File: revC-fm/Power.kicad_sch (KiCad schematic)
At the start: 55 parts, among them Q15 MMDT5551-7-F, Q16 MMDT5551-7-F, Q18 IRF7404TRPBF, Q32 MMBT4403WT1G, SW3 USB Charge Inhibit, SW4 High Inhibit, SW5 High USB Inhibit, SW6 Low Inhibit, U18 TPS54226PWPRPWP14_2P31X2P46-L, U19 ADM1176-1ARMZ-R7, U20 ADM1176-1ARMZ-R7, U21 BQ25883RGER

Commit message: working revC
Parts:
- removed MES1: U70, symbol Device:Ammeter_DC
- removed MES2: U68, symbol Device:Ammeter_DC
- removed R136: CUBESAT LOAD, symbol Device:R_US
- removed SW3: USB Charge Inhibit, symbol Switch:SW_SPST
- removed SW4: High Inhibit, symbol Switch:SW_SPST
- removed SW5: High USB Inhibit, symbol Switch:SW_SPST
- removed SW6: Low Inhibit, symbol Switch:SW_SPST
- added C10, C8, C9: 3.3nF, Capacitor_SMD:C_0603_1608Metric, symbol Device:C
- added R10, R12, R9: 1k, Resistor_SMD:R_0603_1608Metric, symbol Device:R_US
- added R11, R7, R8: 47mR, mainboard-SLI:KRL3216, symbol Device:R_US
- added R27, R6: 150k, Resistor_SMD:R_0603_1608Metric, symbol Device:R_US
- added U5, U8, U9: ADM1176-1ARMZ-R7, mainboard:ADM1176-1ARMZ-R7, symbol mainboard:ADM1176-1ARMZ-R7
- R137, R138: value 0.1 -> 47mR; footprint Resistor_SMD:R_2512_6332Metric -> mainboard-SLI:KRL3216
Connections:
- net 3.3V: now also R10.1, R7.1, U5.2 (SENSE); no longer C61.2, C62.2, L3.2
- net GND: now also C10.1, C8.1, C9.1, R27.1, R6.1, U5.4 (GND), U5.8 (A0), U8.4 (GND), U8.9 (A1), U9.4 (GND)
- net SCL_PWR: now also U5.6 (SCL), U8.6 (SCL), U9.6 (SCL)
- net SDA_PWR: now also U5.7 (SDA), U8.7 (SDA), U9.7 (SDA)
- net VCC_PAYLOAD: now also R8.1, R9.1, U8.2 (SENSE)
- net at U20.8 (A0): now also R27.2
- new net: R9.2, U8.3 (ON)
- new net: C9.2, U8.5 (TIMER)
- new net: R12.2, U9.3 (ON)
- new net: C10.2, U9.5 (TIMER)
- new net: R10.2, U5.3 (ON)
- new net: R6.2, U5.9 (A1)
- new net: C8.2, U5.5 (TIMER)
- new net 3.3Vout: C61.2, C62.2, L3.2, R7.2, U5.1 (VCC)
- new net 5V Payload Regulator/Vout: R8.2, U8.1 (VCC)
- new net 5V RF Regulator/Vout: R11.2, U9.1 (VCC)
- new net 5V_RF: R11.1, R12.1, U9.2 (SENSE), U9.8 (A0), U9.9 (A1)
- no-connect marks 8 -> 11
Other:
- note added: "Addr: 0x41"
- note added: "Addr: 0x42"
- note added: "Addr: 0x43"
- note added: "Addr: 0x44"
- note added: "Addr: 0x48"
- note added: "power to battery node from solar charger"
- note removed: "5V_USB"
- note removed: "Addr: 0x90"
- note removed: "Addr: 0x94"
- note removed: "Current Sense Resistor: 1.0 Ohm is about 0.3mW power lost as heat"
- note removed: "GND"
- note removed: "GNDREF"
- note removed: "SYMBOLIC POWER DIAGRAM"
- note removed: "Solar Reg"
- note removed: "USB Bus Reg"
- note removed: "USB Charge Reg"
- note removed: "USB_RET"
- note removed: "VBATT"
- note removed: "VBUS"
- note removed: "VBUS_INHIBIT"
- note removed: "VBUS_USB"
- note removed: "VCHRG"
- note removed: "VCHRG_USB"
- note removed: "VSOLAR"
- note removed: "VSOLAR_RET"
- note removed: "power TO battery node"
- note removed: "to get battery charging current, subtract u68 current from u68 current"
- moved on the sheet: C61, C62, C63, C64, C65, C66, C67, C68, C69, C70, C71, C72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

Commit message: working revC
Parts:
- added C69, C70: 47uF, Capacitor_SMD:C_1206_3216Metric, symbol Device:C
- C67: renamed from C63; value 100uF -> 47uF; footprint Capacitor_SMD:C_1210_3225Metric -> Capacitor_SMD:C_1206_3216Metric
- C68: renamed from C64; value 100uF -> 47uF; footprint Capacitor_SMD:C_1210_3225Metric -> Capacitor_SMD:C_1206_3216Metric
- Q19: renamed from Q18; value IRF7404TRPBF -> BSZ180P03NS3GATMA1; footprint Package_SO:SOIC-8_3.9x4.9mm_P1.27mm -> mainboard-SLI:PG-TSDSON-8_3.3x3.3mm; symbol mainboard_SLI:IRF7404TRPBF -> mainboard_SLI:BSZ180; Flight IRF7404TRPBF -> (none)
- R23: value 100 -> 1k
- renumbered C69 to C51, C9 to C52, C10 to C53, C70 to C54, C71 to C55, C73 to C56, C68 to C57, C75 to C58, C77 to C59, C76 to C60, C74 to C63, C72 to C64, C67 to C71, C8 to C72, L4 to L3, L3 to L4, Q15 to Q16, Q16 to Q18, R137 to R108, R141 to R109, R8 to R110, R9 to R111, R11 to R112, R12 to R113, R138 to R114, R142 to R115, R27 to R116, R140 to R117, R144 to R118, R147 to R119, R148 to R120, R155 to R121, R149 to R123, R146 to R125, R150 to R126, R151 to R127, R152 to R128, R154 to R129, R145 to R130, R156 to R131, R139 to R132, R143 to R133, R7 to R134, R10 to R135, R6 to R136, U19 to U12, U8 to U13, U9 to U14, U20 to U15, U21 to U16, U18 to U17, U5 to U18
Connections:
- net 3.3V: no longer Q19.2 (S), Q19.3 (S)
- net GND: now also C69.2, C70.2
- net GPS_PWR_IN: no longer Q19.6 (D), Q19.7 (D), Q19.8 (D)
- net VBUS: now also C69.1, C70.1
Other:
- note removed: "16V ceramic 1210 caps"
- moved on the sheet: C61, C62, C67, C68, Q32, R121, R195, R23

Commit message: working revC
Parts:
- removed Q19: BSZ180P03NS3GATMA1, mainboard-SLI:PG-TSDSON-8_3.3x3.3mm, symbol mainboard_SLI:BSZ180
- removed Q32: MMBT4403WT1G, Package_TO_SOT_SMD:SOT-323_SC-70, symbol mainboard-rescue:Q_PNP_BEC-Device-mainboard-rescue
- removed R121: 1Meg, Resistor_SMD:R_0603_1608Metric, symbol Device:R_US
- removed R195: 10Meg, Resistor_SMD:R_0603_1608Metric, symbol Device:R_US
- removed R23: 1k, Resistor_SMD:R_0603_1608Metric, symbol Device:R_US
- L2: renamed from L3; footprint mainboard-SLI:74404032010 -> SierraLobo:74404032010; Flight 74404032010 -> (none); Manufacturer_Part_Number 744316100 -> (none); Proto 744316100 -> (none)
- L3: renamed from L4; footprint mainboard:L_2141 -> SierraLobo:L_2141; Flight SPM5030T-3R3M-HZ -> (none); Manufacturer_Name TAI-TECH -> (none); Manufacturer_Part_Number HPC5040NF-3R3MTH -> (none); Proto HPC5040NF-3R3MTH -> (none)
- Q1: renamed from Q16; symbol mainboard-rescue:MBT2222ADW1T1-Transistor_BJT-mainboard-rescue -> Transistor_BJT:MMDT5551; Flight MMDT5551-7-F -> (none); Manufacturer_Name ON Semiconductor -> (none); Manufacturer_Part_Number MBT2222ADW1T1G -> (none); Proto MBT2222ADW1T1G -> (none)
- Q2: renamed from Q18; symbol mainboard-rescue:MBT2222ADW1T1-Transistor_BJT-mainboard-rescue -> Transistor_BJT:MMDT5551; Flight MMDT5551-7-F -> (none)
- Q2: renamed from Q18; symbol mainboard-rescue:MBT2222ADW1T1-Transistor_BJT-mainboard-rescue -> Transistor_BJT:MMDT5551; Flight MBT2222ADW1T1G -> (none); Manufacturer_Name ON Semiconductor -> (none); Manufacturer_Part_Number MBT2222ADW1T1G -> (none); Proto MBT2222ADW1T1G -> (none)
- R54: renamed from R108; footprint mainboard-SLI:KRL3216 -> SierraLobo:KRL3216
- R56: renamed from R110; footprint mainboard-SLI:KRL3216 -> SierraLobo:KRL3216
- R58: renamed from R112; footprint mainboard-SLI:KRL3216 -> SierraLobo:KRL3216
- R60: renamed from R114; footprint mainboard-SLI:KRL3216 -> SierraLobo:KRL3216
- R77: renamed from R134; footprint mainboard-SLI:KRL3216 -> SierraLobo:KRL3216
- U10: renamed from U12; footprint mainboard:ADM1176-1ARMZ-R7 -> SierraLobo:ADM1176-1ARMZ-R7; symbol mainboard:ADM1176-1ARMZ-R7 -> SierraLobo:ADM1176-1ARMZ-R7; Flight ADM1176-1ARMZ-R7 -> (none); Manufacturer_Name Analog Devices Inc. -> (none); Manufacturer_Part_Number ADM1176-1ARMZ-R7 -> (none); Proto ADM1176-1ARMZ-R7 -> (none)
- U11: renamed from U13; footprint mainboard:ADM1176-1ARMZ-R7 -> SierraLobo:ADM1176-1ARMZ-R7; symbol mainboard:ADM1176-1ARMZ-R7 -> SierraLobo:ADM1176-1ARMZ-R7; Flight ADM1176-1ARMZ-R7 -> (none); Manufacturer_Name Analog Devices Inc. -> (none); Manufacturer_Part_Number ADM1176-1ARMZ-R7 -> (none); Proto ADM1176-1ARMZ-R7 -> (none)
- U12: renamed from U14; footprint mainboard:ADM1176-1ARMZ-R7 -> SierraLobo:ADM1176-1ARMZ-R7; symbol mainboard:ADM1176-1ARMZ-R7 -> SierraLobo:ADM1176-1ARMZ-R7; Flight ADM1176-1ARMZ-R7 -> (none); Manufacturer_Name Analog Devices Inc. -> (none); Manufacturer_Part_Number ADM1176-1ARMZ-R7 -> (none); Proto ADM1176-1ARMZ-R7 -> (none)
- U13: renamed from U15; footprint mainboard:ADM1176-1ARMZ-R7 -> SierraLobo:ADM1176-1ARMZ-R7; symbol mainboard:ADM1176-1ARMZ-R7 -> SierraLobo:ADM1176-1ARMZ-R7; Flight ADM1176-1ARMZ-R7 -> (none); Manufacturer_Name Analog Devices Inc. -> (none); Manufacturer_Part_Number ADM1176-1ARMZ-R7 -> (none); Proto ADM1176-1ARMZ-R7 -> (none)
- U14: renamed from U16; footprint mainboard:QFN50P400X400X100-25N-D -> SierraLobo:QFN50P400X400X100-25N-D; symbol mainboard:BQ25883RGER -> SierraLobo:BQ25883RGER; Flight BQ25883RGER -> (none); Manufacturer_Name Texas Instruments -> (none); Manufacturer_Part_Number BQ25883RGER -> (none); Proto BQ25883RGER -> (none)
- U15: renamed from U17; value TPS54226PWPRPWP14_2P31X2P46-L -> TPS54226PWPR; footprint mainboard:PWP14_2P31X2P46-L -> SierraLobo:PWP14_2P31X2P46-L; symbol mainboard:TPS54226PWPRPWP14_2P31X2P46-L -> SierraLobo:TPS54226PWPR; Flight TPS54226PWPR -> (none); Manufacturer_Name Texas Instruments -> (none); Manufacturer_Part_Number TPS54226PWPR -> (none); Proto TPS54226PWPR -> (none)
- U16: renamed from U18; footprint mainboard:ADM1176-1ARMZ-R7 -> SierraLobo:ADM1176-1ARMZ-R7; symbol mainboard:ADM1176-1ARMZ-R7 -> SierraLobo:ADM1176-1ARMZ-R7; Flight ADM1176-1ARMZ-R7 -> (none); Manufacturer_Name Analog Devices Inc. -> (none); Manufacturer_Part_Number ADM1176-1ARMZ-R7 -> (none); Proto ADM1176-1ARMZ-R7 -> (none)
- renumbered C51 to C29, C52 to C30, C53 to C31, C54 to C32, C55 to C33, C56 to C34, C57 to C35, C58 to C36, C59 to C37, C60 to C38, C61 to C39, C62 to C40, C63 to C41, C64 to C42, C65 to C43, C66 to C44, C67 to C45, C68 to C46, C69 to C47, C70 to C48, C71 to C49, C72 to C50, R109 to R55, R111 to R57, R113 to R59, R115 to R61, R116 to R62, R117 to R63, R118 to R64, R119 to R65, R120 to R66, R123 to R67, R125 to R68, R126 to R69, R127 to R70, R128 to R71, R129 to R72, R130 to R73, R131 to R74, R132 to R75, R133 to R76, R135 to R78, R136 to R79
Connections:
- net 3.3V: now also R77.2; no longer R75.2, R77.1, U15.1 (VO)
- net 3.3Vout: now also R75.2, R77.1, U15.1 (VO); no longer R77.2
- net 5V Payload Regulator/Vout: now also R56.1; no longer R56.2
- net 5V RF Regulator/Vout: now also R58.1; no longer R58.2
- net 5V_RF: now also R58.2; no longer R58.1
- net GND: no longer U11.4 (GND)
- net VCC_PAYLOAD renamed 5V_PYLD
- net 5V_PYLD: now also R56.2; no longer R56.1
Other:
- sheet 5V Payload Regulator ports: added EN, PG, SEN; removed ~{EN}
- sheet 5V RF Regulator ports: added EN, PG, SEN; removed ~{EN}
- note added: "5V Power Monitors"
- note added: "power to VBATT from VCHRG"
- note added: "power to VBUS"
- note removed: "GPS Power Switch"
- note removed: "NOTE: Components labeled "do not install" (DNI) are not populated by default"
- note removed: "power TO bus"
- note removed: "power to battery node from solar charger"
- moved on the sheet: C29, C32, C35, Q1A, Q1B, Q2A, Q2B, R54, R55, R56, R58, R60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

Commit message: routing fm
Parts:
- added D6 (x2): SBRT5A50SA-13, Diode_SMD:D_SMA, symbol mainboard-rescue:D_Schottky-Device-mainboard-rescue
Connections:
- net GND: now also D6.2 (A), D6.2 (A)
- net VBATT: now also D6.1 (K)
- net VBUS_INHIBIT: now also D6.1 (K)
- net 5V Payload Regulator/Vout renamed 5V Payload Regulator/VOUT
- net 5V RF Regulator/Vout renamed 5V RF Regulator/VOUT
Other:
- added sheet Temp Sensor 3 (temp_senkicad_sch.kicad_sch)
- sheet 5V Payload Regulator ports: added TEMP, VIN, VIO, VOUT; removed NTC, SEN, Vout
- sheet 5V RF Regulator ports: added TEMP, VIN, VIO, VOUT; removed NTC, SEN, Vout
- sheet Solar Charge Regulator ports: added BATT_NTC, CHRG, SHDN, TEMP, VCHRG, VIN, VIO; removed none
- moved on the sheet: C29, C32, R54, R55, R60, R61, R62, U10, U13

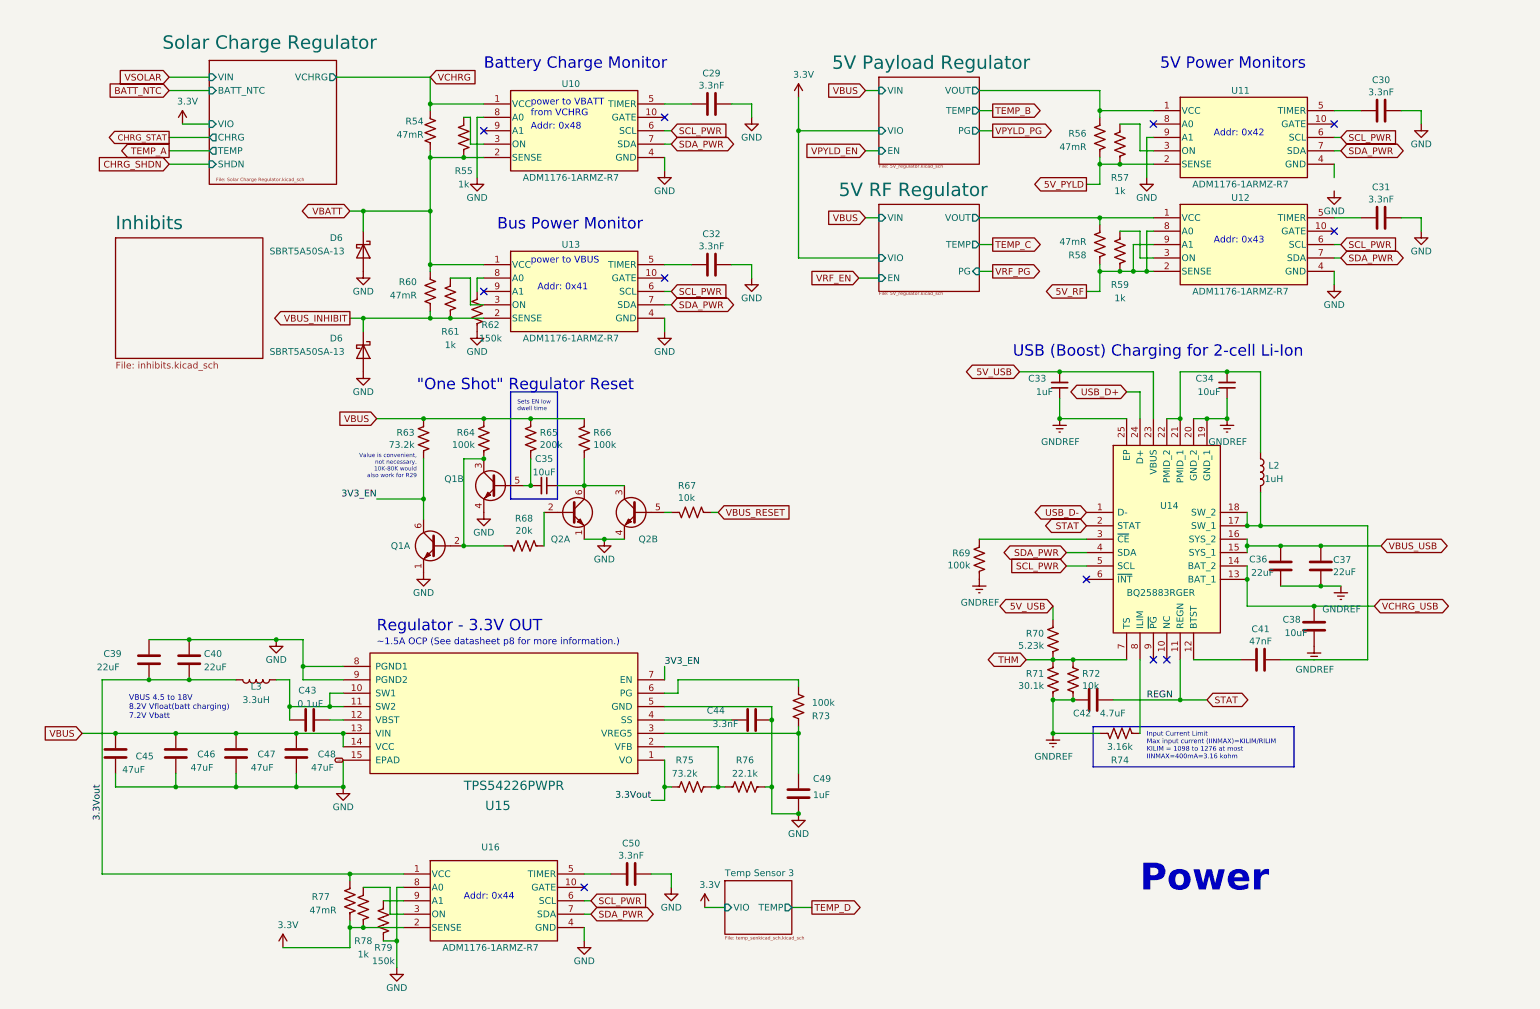
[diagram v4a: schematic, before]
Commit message: updated analog , solar comp, layout
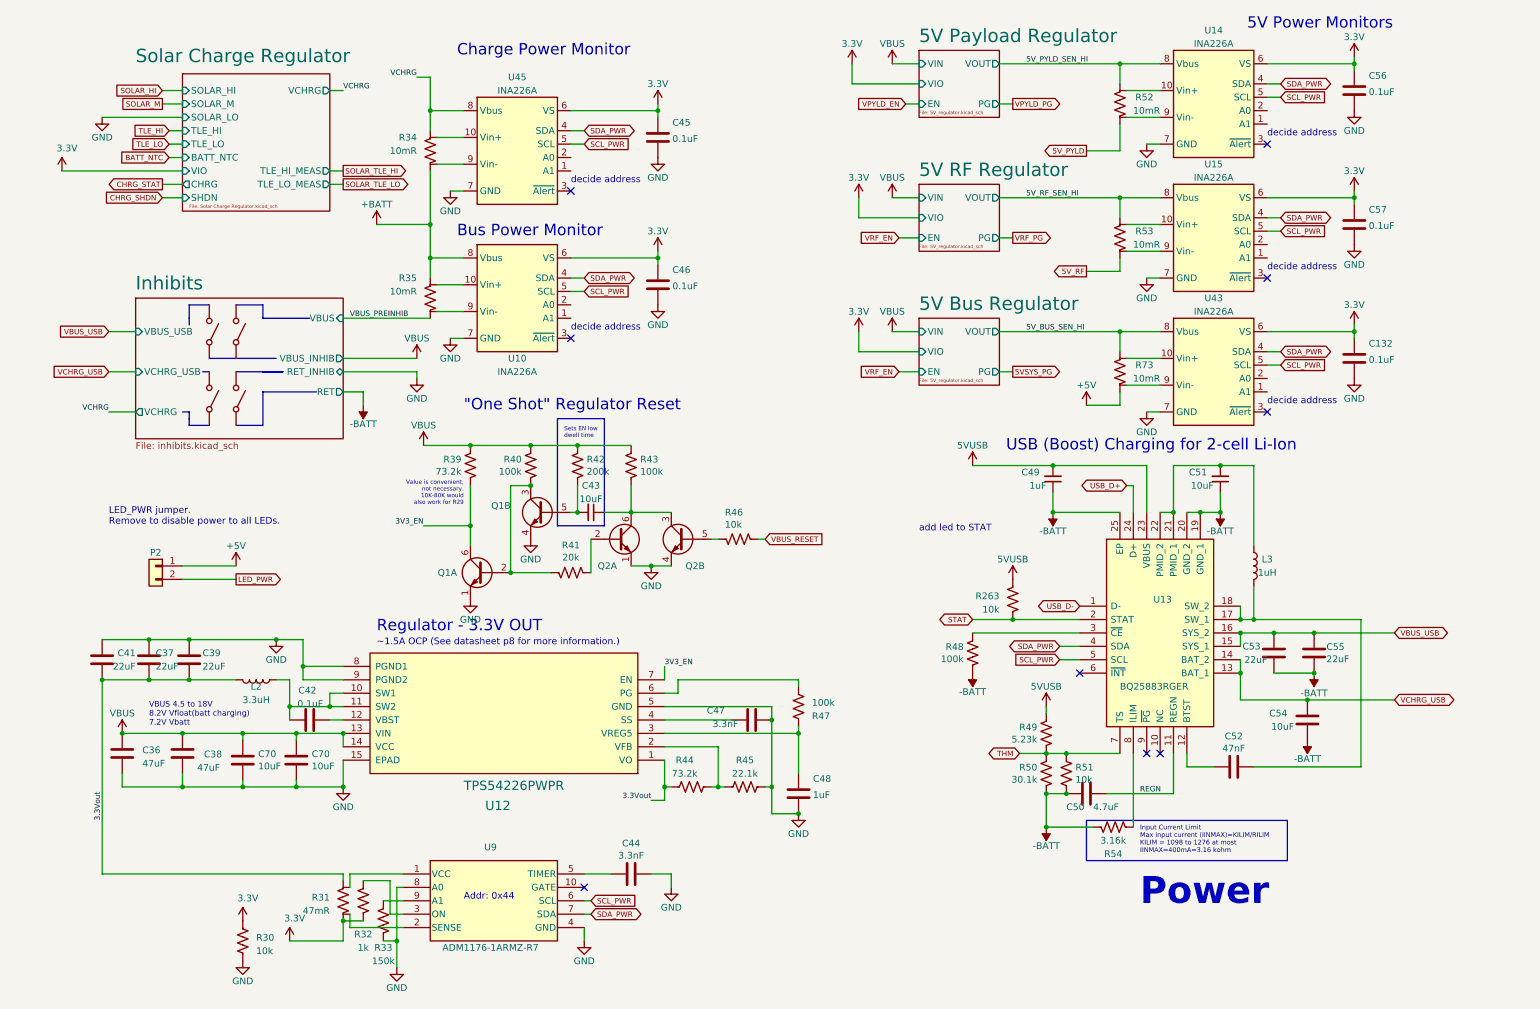
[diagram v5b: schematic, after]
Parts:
- removed C29, C30, C31, C32: 3.3nF, Capacitor_SMD:C_0603_1608Metric, symbol Device:C
- removed C47, C48: 47uF, Capacitor_SMD:C_1206_3216Metric, symbol Device:C
- removed D6 (x2): SBRT5A50SA-13, Diode_SMD:D_SMA, symbol mainboard-rescue:D_Schottky-Device-mainboard-rescue
- removed R55, R57, R59, R61: 1k, Resistor_SMD:R_0603_1608Metric, symbol Device:R_US
- removed R62: 150k, Resistor_SMD:R_0603_1608Metric, symbol Device:R_US
- removed U10, U11, U12, U13: ADM1176-1ARMZ-R7, SierraLobo:ADM1176-1ARMZ-R7, symbol SierraLobo:ADM1176-1ARMZ-R7
- added C132, C45, C46, C56, C57: 0.1uF, Capacitor_SMD:C_0402_1005Metric, symbol Device:C
- added C41: 22uF, Capacitor_SMD:C_0805_2012Metric, symbol Device:C
- added C70 (x2): 10uF, Capacitor_SMD:C_0805_2012Metric, symbol Device:C
- added P2: TSM-102-01-L-SV-P-TR, Connector_PinHeader_2.54mm:PinHeader_1x02_P2.54mm_Vertical_SMD_Pin1Right, symbol Connector_Generic:Conn_01x02
- added R263, R30: 10k, Resistor_SMD:R_0603_1608Metric, symbol Device:R_US
- added R73: 10mR, SierraLobo:KRL3216, symbol SierraLobo:R_US_SENSE
- added SW3, SW4, SW5, SW6: SW_SPST, symbol Switch:SW_SPST
- added U10, U14, U15, U43, U45: INA226A, Package_SO:VSSOP-10_3x3mm_P0.5mm, symbol SierraLobo:INA226A
- C42: renamed from C43; footprint Capacitor_SMD:C_0603_1608Metric -> Capacitor_SMD:C_0402_1005Metric
- C44: renamed from C50; footprint Capacitor_SMD:C_0603_1608Metric -> Capacitor_SMD:C_0402_1005Metric
- C47: renamed from C44; footprint Capacitor_SMD:C_0603_1608Metric -> Capacitor_SMD:C_0402_1005Metric
- C52: renamed from C41; footprint Capacitor_SMD:C_0603_1608Metric -> Capacitor_SMD:C_0402_1005Metric
- L2: renamed from L3; footprint SierraLobo:L_2141 -> Inductor_SMD:L_Wuerth_HCI-5040
- R31: renamed from R77; symbol Device:R_US -> SierraLobo:R_US_SENSE
- R34: renamed from R54; value 47mR -> 10mR; symbol Device:R_US -> SierraLobo:R_US_SENSE
- R35: renamed from R60; value 47mR -> 10mR; symbol Device:R_US -> SierraLobo:R_US_SENSE
- R52: renamed from R56; value 47mR -> 10mR; symbol Device:R_US -> SierraLobo:R_US_SENSE
- R53: renamed from R58; value 47mR -> 10mR; symbol Device:R_US -> SierraLobo:R_US_SENSE
- renumbered C45 to C36, C39 to C37, C46 to C38, C40 to C39, C35 to C43, C49 to C48, C33 to C49, C42 to C50, C34 to C51, C36 to C53, C38 to C54, C37 to C55, L2 to L3, R78 to R32, R79 to R33, R63 to R39, R64 to R40, R68 to R41, R65 to R42, R66 to R43, R75 to R44, R76 to R45, R67 to R46, R73 to R47, R69 to R48, R70 to R49, R71 to R50, R72 to R51, R74 to R54, U15 to U12, U14 to U13, U16 to U9
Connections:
- net 5V Payload Regulator/VOUT is gone; now on net 5V_PYLD: R52.1
- net 5V RF Regulator/VOUT is gone; now on net 5V_RF: R53.1
- net 3.3V: now also R31.1, C132.1, C45.1, C46.1, C56.1, C57.1, R30.1, U10.6 (VS), U14.6 (VS), U15.6 (VS), U43.6 (VS), U45.6 (VS); no longer R31.2, U9.2 (SENSE)
- net 3.3Vout: now also R31.2, C41.2; no longer R31.1, U9.1 (VCC)
- net 5V_PYLD: no longer R52.2
- net 5V_RF: no longer R53.2
- net GND: now also C132.2, C41.1, C45.2, C46.2, C56.2, C57.2, C70.2, C70.2, R30.2, U10.7 (GND), U14.7 (GND), U15.7 (GND), U43.7 (GND), U45.7 (GND)
- net SCL_PWR: now also U10.5 (SCL), U14.5 (SCL), U15.5 (SCL), U43.5 (SCL), U45.5 (SCL)
- net SDA_PWR: now also U10.4 (SDA), U14.4 (SDA), U15.4 (SDA), U43.4 (SDA), U45.4 (SDA)
- net STAT: now also R263.1; no longer C50.1, U13.11 (REGN)
- net VBUS: now also C70.1, C70.1
- net VCHRG: now also U45.8 (Vbus)
- net 5V_USB renamed +5V
- net +5V: now also P2.1 (Pin_1), R263.2, R73.1
- net GNDREF renamed -BATT
- net VBATT renamed +BATT
- net +BATT: now also U10.8 (Vbus)
- net VBUS_INHIBIT renamed VBUS_PREINHIB
- new net: R35.3, U10.9 (Vin-)
- new net: R35.4, U10.10 (Vin+)
- new net: R34.3, U45.9 (Vin-)
- new net: R34.4, U45.10 (Vin+)
- new net: R52.4, U14.10 (Vin+)
- new net: R52.3, U14.9 (Vin-)
- new net: R73.3, U43.9 (Vin-)
- new net: R73.4, U43.10 (Vin+)
- new net: R53.4, U15.10 (Vin+)
- new net: R53.3, U15.9 (Vin-)
- new net: R31.3, U9.2 (SENSE)
- new net: R31.4, U9.1 (VCC)
- new net 5V_BUS_SEN_HI: R73.2, U43.8 (Vbus)
- new net 5V_PYLD_SEN_HI: R52.2, U14.8 (Vbus)
- new net 5V_RF_SEN_HI: R53.2, U15.8 (Vbus)
- new net LED_PWR: P2.2 (Pin_2)
- new net REGN: C50.1, U13.11 (REGN)
- no-connect marks 11 -> 9
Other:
- removed sheet Temp Sensor 3
- added sheet 5V Bus Regulator (5V_regulator.kicad_sch)
- sheet 5V Payload Regulator ports: added none; removed TEMP
- sheet 5V RF Regulator ports: added none; removed TEMP
- sheet Inhibits ports: added RET, RET_INHIB, VBUS, VBUS_INHIB, VBUS_USB, VCHRG, VCHRG_USB; removed none
- sheet Solar Charge Regulator ports: added SOLAR_HI, SOLAR_LO, SOLAR_M, TLE_HI, TLE_HI_MEAS, TLE_LO, TLE_LO_MEAS; removed TEMP, VIN
- note added: "Charge Power Monitor"
- note added: "LED_PWR jumper. Remove to disable power to all LEDs."
- note added: "add led to STAT"
- note added: "decide address"
- note removed: "Addr: 0x41"
- note removed: "Addr: 0x42"
- note removed: "Addr: 0x43"
- note removed: "Addr: 0x48"
- note removed: "Battery Charge Monitor"
- note removed: "power to VBATT from VCHRG"
- note removed: "power to VBUS"
- moved on the sheet: C36, C38, C43, C49, C50, C51, C52, C53, C54, C55, L3, Q1A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
